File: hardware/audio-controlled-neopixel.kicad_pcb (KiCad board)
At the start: 2 copper layers, 96 x 56 mm, 61 parts, among them J1 AudioJack4, J2 AudioJack4, J3 KF2EDGK, J4 KF2EDGK, J5 KF2EDGK, J6 Conn_01x01_Female, J7 Conn_01x01_Female, J8 Conn_01x01_Female, J9 Conn_01x01_Female, SW1 SW_SPST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

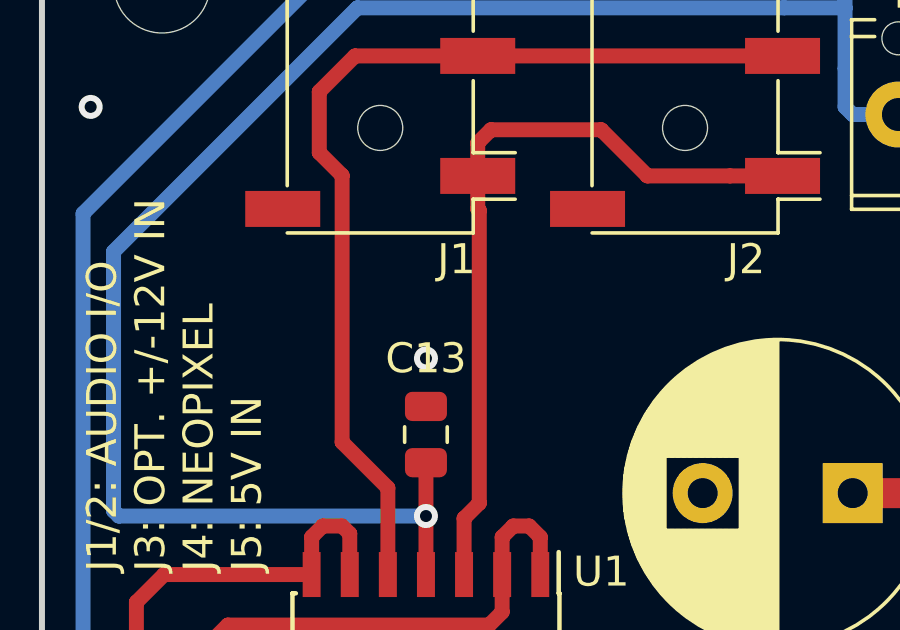
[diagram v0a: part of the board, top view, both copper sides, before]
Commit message: added input resistors
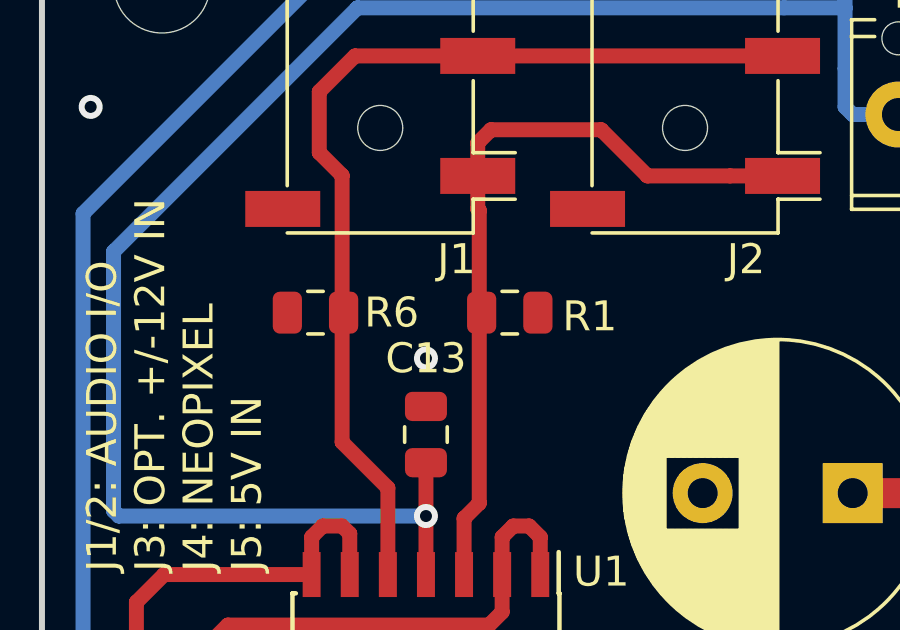
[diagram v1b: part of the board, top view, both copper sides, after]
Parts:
- added R1: 10K, Resistor_SMD:R_0805_2012Metric, F.Cu at (53.6, 43.9)
- added R6: 10K, Resistor_SMD:R_0805_2012Metric, F.Cu at (47.1, 43.9)
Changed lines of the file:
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@@
-(kicad_pcb (version 20171130) (host pcbnew 5.0.2-bee76a0~70~ubuntu18.04.1)
+(kicad_pcb (version 20171130) (host pcbnew "(5.0.2)-1")
   (general
     (thickness 1.6)
@@
     (tracks 319)
     (zones 0)
-    (modules 61)
+    (modules 63)
     (nets 66)
   )
@@
     (add_net "Net-(U3-Pad13)")
   )
+  (module Resistor_SMD:R_0805_2012Metric (layer F.Cu)
+    (at 53.594 43.942 180)
+    (descr "Resistor SMD 0805 (2012 Metric), square (rectangular) end terminal, IPC_7351 nominal, (Body size source: https://docs.google.com/spreadsheets/d/1BsfQQcO9C6DZCsRaXUlFlo91Tg2WpOkGARC1WS5S8t0/edit?usp=sharing), generated with kicad-footprint-generator")
+    (tags resistor)
+    (attr smd)
+    (fp_text reference R1 (at -2.667 -0.127 180) (layer F.SilkS)
+      (effects (font (size 1 1) (thickness 0.15)))
+    )
+    (fp_text value 10K (at 0 1.65 180) (layer F.Fab)
+      (effects (font (size 1 1) (thickness 0.15)))
+    )
+    (fp_text user %R (at 0 0 180) (layer F.Fab)
+      (effects (font (size 0.5 0.5) (thickness 0.08)))
+    )
+    (fp_line (start 1.68 0.95) (end -1.68 0.95) (layer F.CrtYd) (width 0.05))
+    (fp_line (start 1.68 -0.95) (end 1.68 0.95) (layer F.CrtYd) (width 0.05))
+    (fp_line (start -1.68 -0.95) (end 1.68 -0.95) (layer F.CrtYd) (width 0.05))
+    (fp_line (start -1.68 0.95) (end -1.68 -0.95) (layer F.CrtYd) (width 0.05))
+    (fp_line (start -0.258578 0.71) (end 0.258578 0.71) (layer F.SilkS) (width 0.12))
+    (fp_line (start -0.258578 -0.71) (end 0.258578 -0.71) (layer F.SilkS) (width 0.12))
+    (fp_line (start 1 0.6) (end -1 0.6) (layer F.Fab) (width 0.1))
+    (fp_line (start 1 -0.6) (end 1 0.6) (layer F.Fab) (width 0.1))
+    (fp_line (start -1 -0.6) (end 1 -0.6) (layer F.Fab) (width 0.1))
+    (fp_line (start -1 0.6) (end -1 -0.6) (layer F.Fab) (width 0.1))
+    (pad 2 smd roundrect (at 0.9375 0 180) (size 0.975 1.4) (layers F.Cu F.Paste F.Mask) (roundrect_rratio 0.25)
+      (net 44 /Input_R))
+    (pad 1 smd roundrect (at -0.9375 0 180) (size 0.975 1.4) (layers F.Cu F.Paste F.Mask) (roundrect_rratio 0.25)
+      (net 1 GND))
+    (model ${KISYS3DMOD}/Resistor_SMD.3dshapes/R_0805_2012Metric.wrl
+      (at (xyz 0 0 0))
+      (scale (xyz 1 1 1))
+      (rotate (xyz 0 0 0))
+    )
+  )
+  (module Resistor_SMD:R_0805_2012Metric (layer F.Cu)
+    (at 47.117 43.942)
+    (descr "Resistor SMD 0805 (2012 Metric), square (rectangular) end terminal, IPC_7351 nominal, (Body size source: https://docs.google.com/spreadsheets/d/1BsfQQcO9C6DZCsRaXUlFlo91Tg2WpOkGARC1WS5S8t0/edit?usp=sharing), generated with kicad-footprint-generator")
+    (tags resistor)
+    (attr smd)
+    (fp_text reference R6 (at 2.54 0) (layer F.SilkS)
+      (effects (font (size 1 1) (thickness 0.15)))
+    )
+    (fp_text value 10K (at 0 1.65) (layer F.Fab)
+      (effects (font (size 1 1) (thickness 0.15)))
+    )
+    (fp_line (start -1 0.6) (end -1 -0.6) (layer F.Fab) (width 0.1))
+    (fp_line (start -1 -0.6) (end 1 -0.6) (layer F.Fab) (width 0.1))
+    (fp_line (start 1 -0.6) (end 1 0.6) (layer F.Fab) (width 0.1))
+    (fp_line (start 1 0.6) (end -1 0.6) (layer F.Fab) (width 0.1))
+    (fp_line (start -0.258578 -0.71) (end 0.258578 -0.71) (layer F.SilkS) (width 0.12))
+    (fp_line (start -0.258578 0.71) (end 0.258578 0.71) (layer F.SilkS) (width 0.12))
+    (fp_line (start -1.68 0.95) (end -1.68 -0.95) (layer F.CrtYd) (width 0.05))
+    (fp_line (start -1.68 -0.95) (end 1.68 -0.95) (layer F.CrtYd) (width 0.05))
+    (fp_line (start 1.68 -0.95) (end 1.68 0.95) (layer F.CrtYd) (width 0.05))
+    (fp_line (start 1.68 0.95) (end -1.68 0.95) (layer F.CrtYd) (width 0.05))
+    (fp_text user %R (at 0 0) (layer F.Fab)
+      (effects (font (size 0.5 0.5) (thickness 0.08)))
+    )
+    (pad 1 smd roundrect (at -0.9375 0) (size 0.975 1.4) (layers F.Cu F.Paste F.Mask) (roundrect_rratio 0.25)
+      (net 1 GND))
+    (pad 2 smd roundrect (at 0.9375 0) (size 0.975 1.4) (layers F.Cu F.Paste F.Mask) (roundrect_rratio 0.25)
+      (net 45 /Input_L))
+    (model ${KISYS3DMOD}/Resistor_SMD.3dshapes/R_0805_2012Metric.wrl
+      (at (xyz 0 0 0))
+      (scale (xyz 1 1 1))
+      (rotate (xyz 0 0 0))
+    )
+  )
   (module Footprints:TMAxxxxD (layer F.Cu)

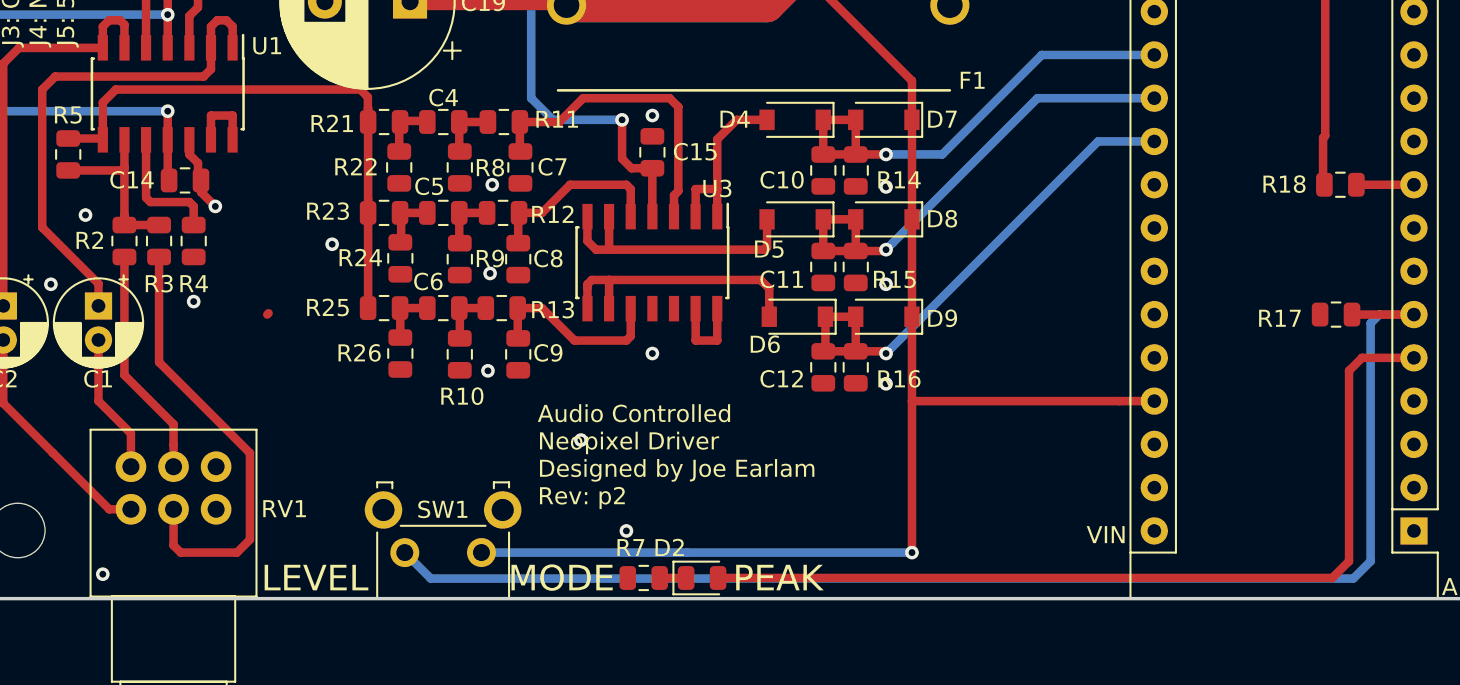
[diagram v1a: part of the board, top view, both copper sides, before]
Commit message: connect both op-amps to dual supply
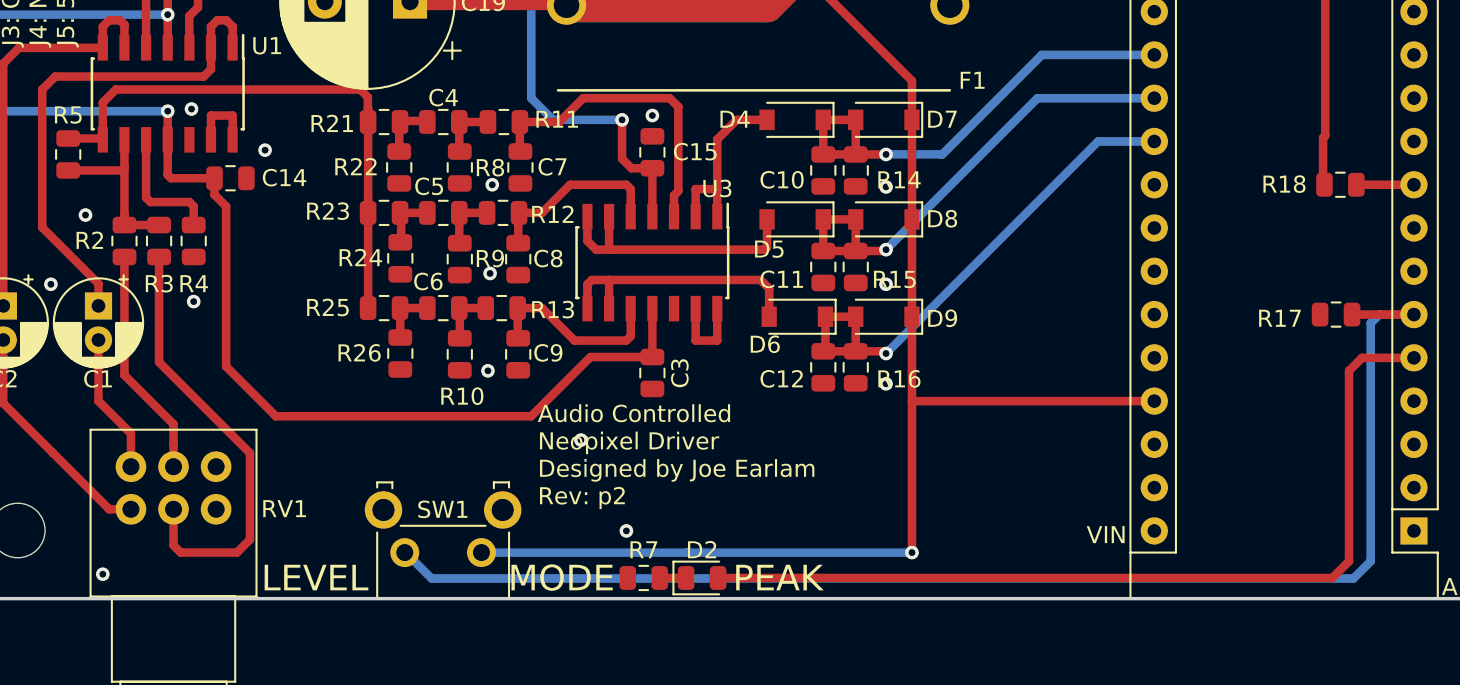
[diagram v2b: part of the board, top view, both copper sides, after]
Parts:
- added C3: 100n, Capacitor_SMD:C_0805_2012Metric, F.Cu at (79.2, 71.8)
- R1, R6: value 10K -> 100K
- R10, R12: value 7K5 -> 8K2
- moved C14 2.67 mm to (54.5, 60.3)
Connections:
- net /Buf_input renamed Net-(R21-Pad2)
- U3 pad 11: GND -> -12V
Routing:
- net -12V: track 131.9 -> 176.6 mm
- net GND: track 5.45 -> 0.00 mm, vias 18 -> 17

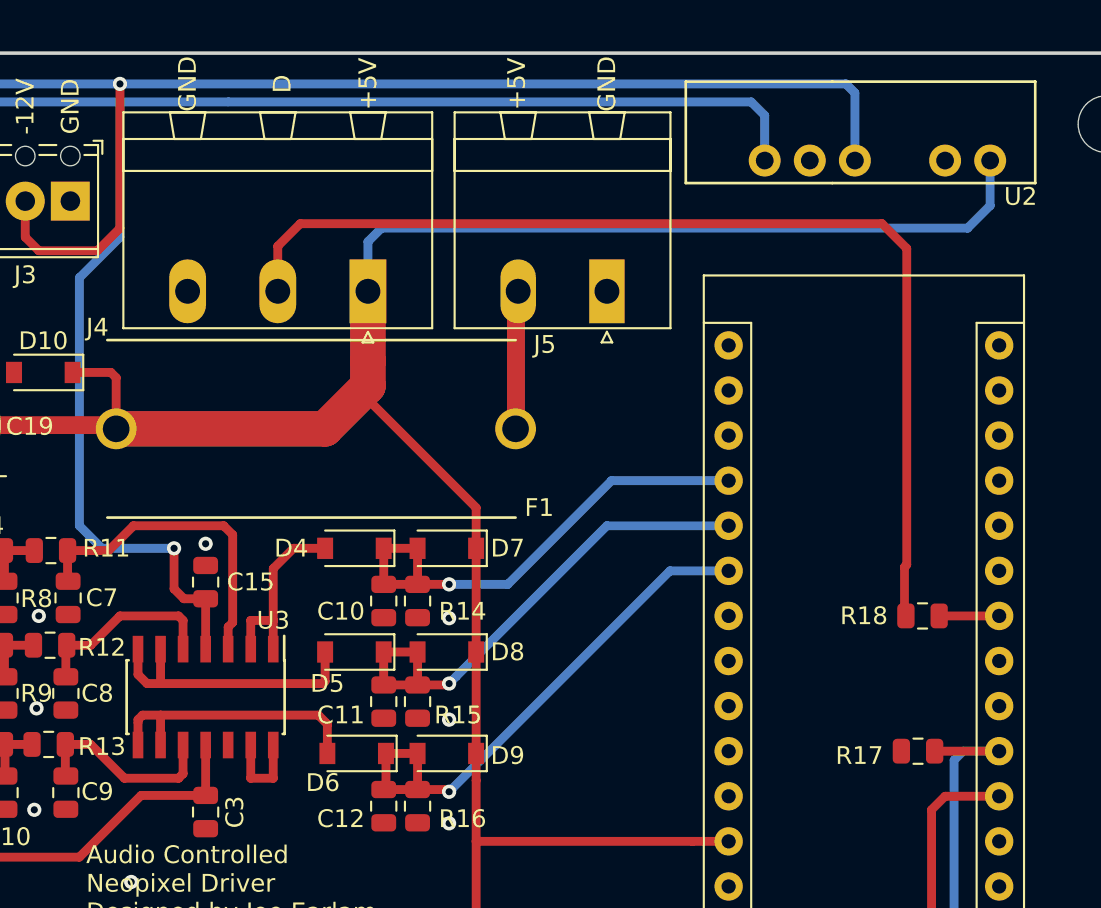
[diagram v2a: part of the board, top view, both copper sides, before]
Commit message: adjusted component values for better real world performance, changed diode types, minor PCB changes for better ground return paths
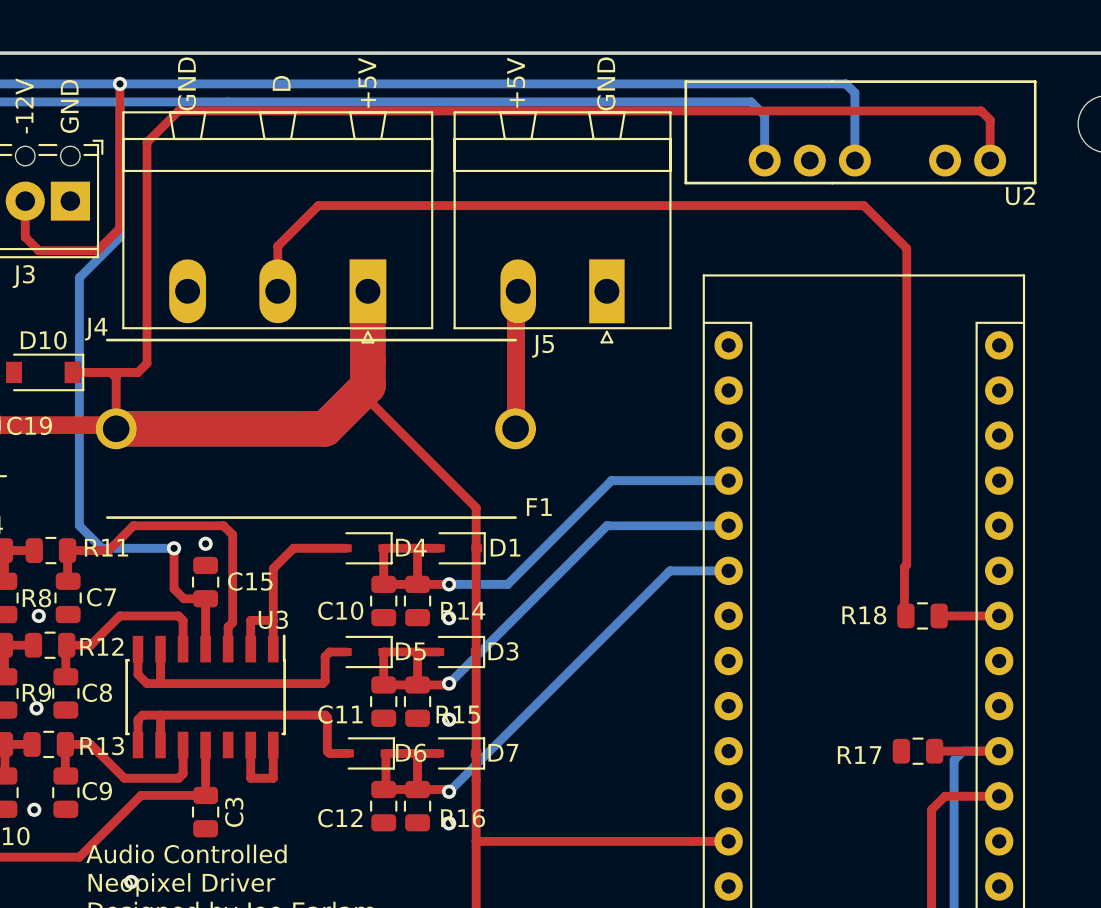
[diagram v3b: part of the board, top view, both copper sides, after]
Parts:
- removed D8, D9: 1N5819, Diode_SMD:D_SOD-123
- added D1: BAT20JFILM, Diode_SMD:D_SOD-323, F.Cu at (93.5, 56.9)
- added D3: BAT20JFILM, Diode_SMD:D_SOD-323, F.Cu at (93.4, 62.7)
- D4, D5, D6: value 1N4148 -> BAT20JFILM; footprint Diode_SMD:D_SOD-123 -> Diode_SMD:D_SOD-323
- D7: value 1N5819 -> BAT20JFILM; footprint Diode_SMD:D_SOD-123 -> Diode_SMD:D_SOD-323
- moved D7 11.6 mm to (93.4, 68.5)
- moved D5 0.60 mm to (88.2, 62.7)
- moved D4 0.60 mm to (88.2, 56.9)
- moved D6 0.60 mm to (88.4, 68.5)
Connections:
- D7 pad 2: /Low -> /High
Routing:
- net +5V: track 173.0 -> 197.7 mm
- net /Low: track 27.8 -> 29.3 mm
- net Net-(D6-Pad2): track 15.7 -> 17.1 mm
- net Net-(D4-Pad2): track 10.8 -> 12.0 mm
- net /High: track 30.5 -> 31.7 mm
- net /Mid: track 28.8 -> 30.0 mm
- net Net-(D5-Pad2): track 15.8 -> 16.9 mm
- net /Neopixel: track 60.0 -> 60.8 mm

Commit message: hardware updates
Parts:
- removed C2: 10u, Capacitor_THT:CP_Radial_D5.0mm_P2.00mm
- removed R17: 10K, Resistor_SMD:R_0805_2012Metric
- removed R21, R23: 100K, Resistor_SMD:R_0805_2012Metric
- removed R22: 250K, Resistor_SMD:R_0805_2012Metric
- removed R24: 169K, Resistor_SMD:R_0805_2012Metric
- removed R25: 0R, Resistor_SMD:R_0805_2012Metric
- removed R26: NF, Resistor_SMD:R_0805_2012Metric
- added J10: Conn_01x04_Male, Connector_PinHeader_2.54mm:PinHeader_1x04_P2.54mm_Vertical, F.Cu at (129.8, 40.6)
- added R19: 10K, Resistor_SMD:R_0805_2012Metric, F.Cu at (51.8, 64.1)
- added R20: 200K, Resistor_SMD:R_0805_2012Metric, F.Cu at (51.8, 62.1)
- added RV2: 5K, Potentiometer_SMD:Potentiometer_Vishay_TS53YJ_Vertical, F.Cu at (66.7, 58.9)
- added RV3: 5K, Potentiometer_SMD:Potentiometer_Vishay_TS53YJ_Vertical, F.Cu at (66.7, 64.8)
- added RV4: 5K, Potentiometer_SMD:Potentiometer_Vishay_TS53YJ_Vertical, F.Cu at (66.7, 70.6)
- C19: footprint Capacitor_THT:CP_Radial_D10.0mm_P5.00mm -> Capacitor_SMD:CP_Elec_10x10
- J1, J2: footprint Connector_Audio:Jack_3.5mm_PJ320D_Horizontal -> custom:Jack_3.5mm_PJ320D_Horizontal
- R5: value 200K -> 10K
- RV1: value 10KA -> R_POT; footprint Potentiometer_THT:Potentiometer_Alps_RK097_Dual_Horizontal -> Potentiometer_THT:Potentiometer_Alps_RK097_Single_Horizontal
- U1: value LM324 -> LM358; footprint Package_SO:SOIC-14_3.9x8.7mm_P1.27mm -> Package_SO:SOIC-8_3.9x4.9mm_P1.27mm
- moved R2 17.6 mm to (52.6, 47.0), turned to 270 degrees
- moved R3 17.0 mm to (50.5, 47.0), turned to 90 degrees
- moved R5 11.8 mm to (53.5, 50.8), turned to 180 degrees
- moved R4 9.67 mm to (47.5, 55.6), turned to 180 degrees
- moved F1 7.62 mm to (92.3, 50.3)
- moved D10 7.56 mm to (77.6, 48.0), turned to 0 degrees
- moved C8 5.33 mm to (76.7, 65.1)
- moved C9 5.33 mm to (76.7, 70.7)
- moved D1 5.33 mm to (98.8, 56.9)
- moved D3 5.33 mm to (98.8, 62.7)
- moved D5 5.33 mm to (93.6, 62.7)
- moved D6 5.33 mm to (93.7, 68.5)
- moved D7 5.33 mm to (98.8, 68.5)
- moved R10 5.33 mm to (73.3, 70.7)
- moved R11 5.33 mm to (75.9, 57.0)
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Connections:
- A1 pad 27: +5V -> Net-(A1-Pad27)
- R2 pad 1: Net-(R2-Pad1) -> /Input_R
- R3 pad 2: Net-(R3-Pad2) -> /Input_L
- R5 pad 1: Net-(R21-Pad2) -> Net-(C1-Pad2)
- R6 pad 1: GND -> /Input_L
- R6 pad 2: /Input_L -> GND
- RV1 pad 1: Net-(C2-Pad2) -> GND
- RV1 pad 2: Net-(R3-Pad2) -> Net-(RV1-Pad2)
- RV1 pad 3: GND -> Net-(C1-Pad1)
- SW1 pad 1: +5V -> GND
- U1 pad 1: Net-(C1-Pad1) -> Net-(C1-Pad2)
- U1 pad 2: Net-(C1-Pad1) -> Net-(R2-Pad2)
- U1 pad 3: /Input_R -> Net-(R4-Pad1)
- U1 pad 5: /Input_L -> Net-(RV1-Pad2)
- U1 pad 6: Net-(C2-Pad1) -> Net-(R19-Pad1)
- U1 pad 7: Net-(C2-Pad1) -> Net-(R20-Pad1)
- U1 pad 8: Net-(R21-Pad2) -> -12V
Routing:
- net +5V: track 197.7 -> 140.6 mm, vias 1 -> 0
- net Net-(A1-Pad30): track 0.00 -> 56.8 mm
- net Net-(A1-Pad27): track 0.00 -> 49.2 mm
- net Net-(R20-Pad1): track 0.00 -> 42.3 mm
- net +12V: track 144.2 -> 184.0 mm, vias 2 -> 3
- net Net-(R21-Pad2): track 32.7 -> 0.00 mm
- net Net-(R3-Pad2): track 25.9 -> 0.00 mm
- net Net-(C2-Pad1): track 24.6 -> 0.00 mm
- net Net-(RV1-Pad2): track 0.00 -> 22.0 mm
- net Net-(C1-Pad2): track 8.23 -> 23.7 mm
- net Net-(C2-Pad2): track 13.8 -> 0.00 mm
- net Net-(R2-Pad1): track 13.5 -> 0.00 mm
- net -12V: track 176.6 -> 189.6 mm
- net /Input_L: track 33.0 -> 20.6 mm
- net /Input_R: track 25.6 -> 16.1 mm
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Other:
- board text added: "12V 5V"
- board text added: "ARDUINO POWER SELECTION"
- board text added: "Audio Controlled Neopixel Driver Designed by Joe Earlam Rev: 3"
- board text added: "HIGH"
- board text added: "LOW"
- board text added: "MID"
- board text removed: "Audio Controlled Neopixel Driver Designed by Joe Earlam Rev: p2"
